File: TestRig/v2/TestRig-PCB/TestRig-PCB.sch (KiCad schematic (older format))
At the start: 1 part

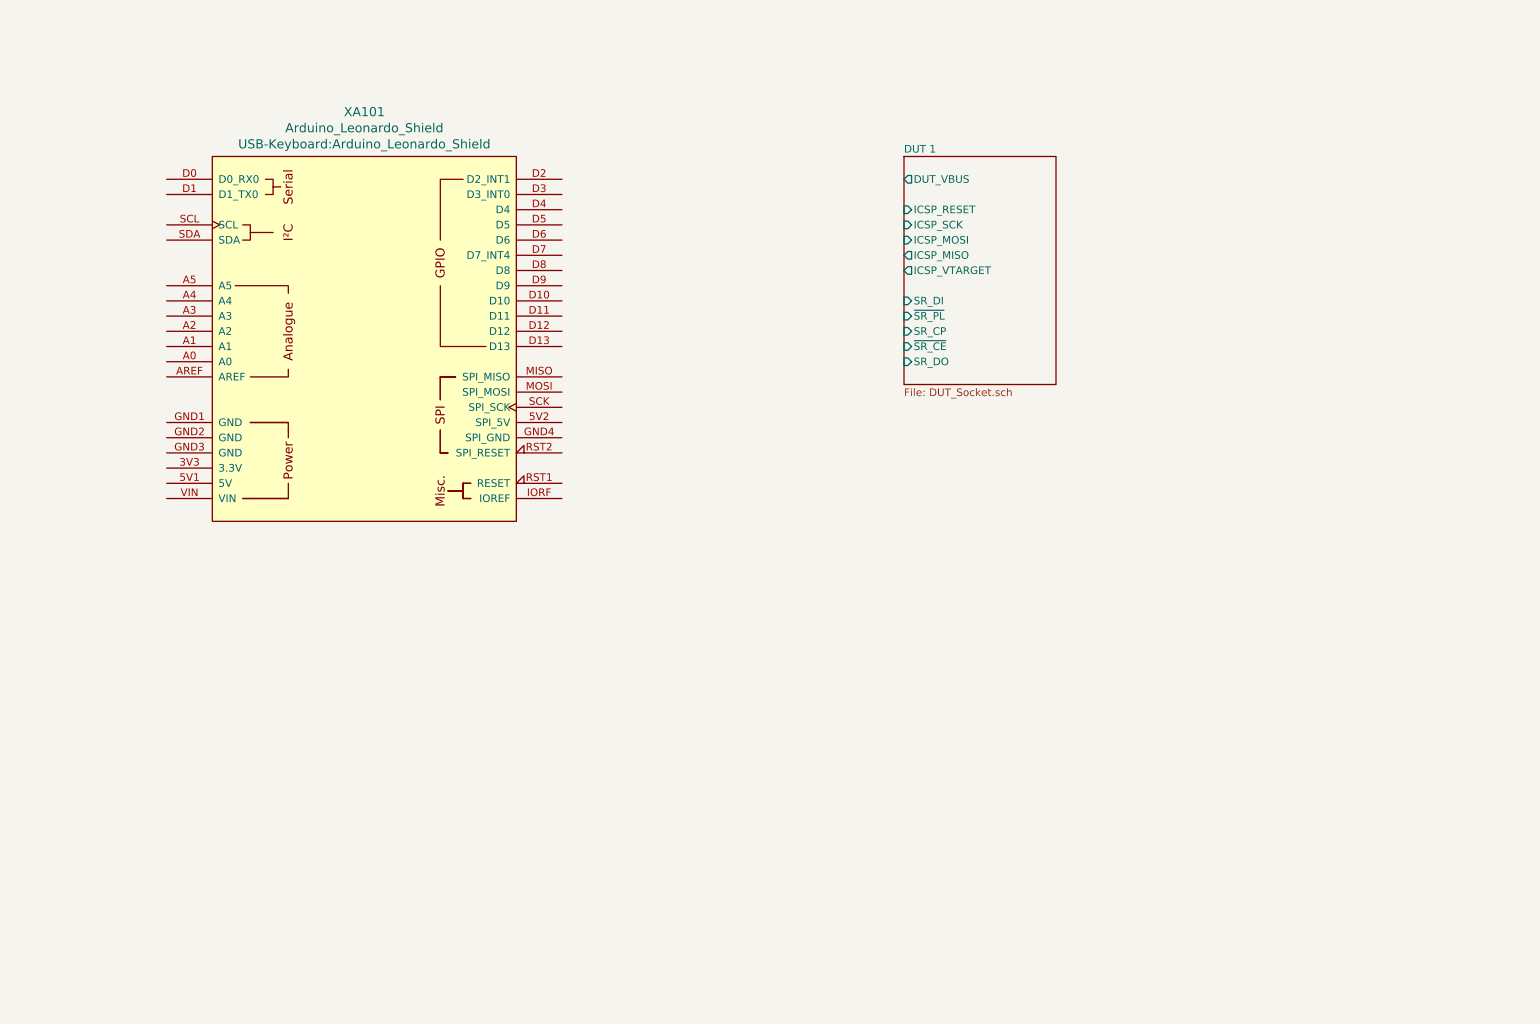
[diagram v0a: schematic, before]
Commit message: Adds working test rig
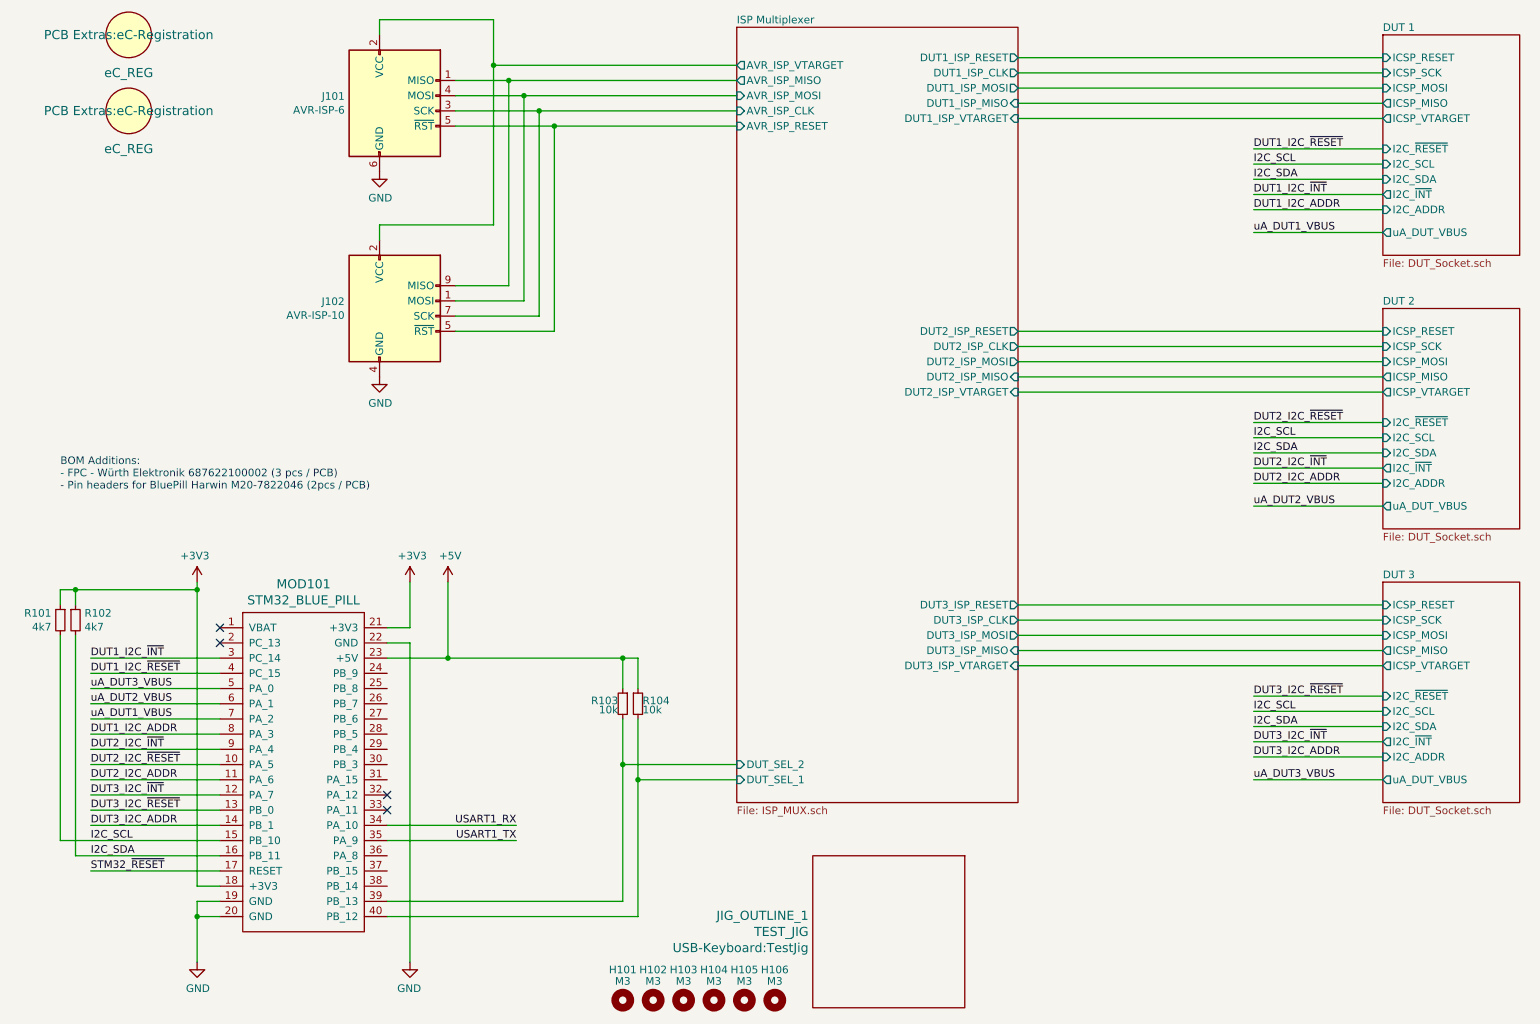
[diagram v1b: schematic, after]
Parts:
- removed XA101: Arduino_Leonardo_Shield, USB-Keyboard:Arduino_Leonardo_Shield, symbol arduino:Arduino_Leonardo_Shield
- added H101, H102, H103, H104, H105, H106: M3, MountingHole:MountingHole_3.2mm_M3, symbol Mechanical:MountingHole
- added J101: AVR-ISP-6, Connector_IDC:IDC-Header_2x03_P2.54mm_Vertical, symbol Connector:AVR-ISP-6
- added J102: AVR-ISP-10, Connector_IDC:IDC-Header_2x05_P2.54mm_Vertical, symbol Connector:AVR-ISP-10
- added JIG_OUTLINE_1: TEST_JIG, USB-Keyboard:TestJig, symbol rbv_pcb_extras:PCB_OUTLINE
- added MOD101: STM32_BLUE_PILL, BluePill:STM32F103C8T6-ARM-BOARD, symbol I2C-HID-Keyboard-rescue:STM32F103C8T6_BOARD
- added R101, R102: 4k7, Resistor_SMD:R_0603_1608Metric, symbol Device:R_Small
- added R103, R104: 10k, Resistor_SMD:R_0603_1608Metric, symbol Device:R_Small
- added REG101, REG102: eC_REG, PCB Extras:eC-Registration, symbol rbv_pcb_extras:DUMMY_KEY
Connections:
- new net +3V3: MOD101.18 (+3V3), MOD101.21 (+3V3), R101.1, R102.1
- new net +5V: MOD101.23 (+5V), R103.1, R104.1
- new net DUT1_I2C_ADDR: MOD101.8 (PA_3)
- new net DUT1_I2C_~INT: MOD101.3 (PC_14)
- new net DUT1_I2C_~RESET: MOD101.4 (PC_15)
- new net DUT2_I2C_ADDR: MOD101.11 (PA_6)
- new net DUT2_I2C_~INT: MOD101.9 (PA_4)
- new net DUT2_I2C_~RESET: MOD101.10 (PA_5)
- new net DUT3_I2C_ADDR: MOD101.14 (PB_1)
- new net DUT3_I2C_~INT: MOD101.12 (PA_7)
- new net DUT3_I2C_~RESET: MOD101.13 (PB_0)
- new net GND: J101.6 (GND), J102.10 (GND), J102.4 (GND), J102.6 (GND), J102.8 (GND), MOD101.19 (GND), MOD101.20 (GND), MOD101.22 (GND)
- new net I2C_SCL: MOD101.15 (PB_10), R101.2
- new net I2C_SDA: MOD101.16 (PB_11), R102.2
- new net ISP Multiplexer/AVR_ISP_CLK: J101.3 (SCK), J102.7 (SCK)
- new net ISP Multiplexer/AVR_ISP_MISO: J101.1 (MISO), J102.9 (MISO)
- new net ISP Multiplexer/AVR_ISP_MOSI: J101.4 (MOSI), J102.1 (MOSI)
- new net ISP Multiplexer/AVR_ISP_RESET: J101.5 (~RST), J102.5 (~RST)
- new net ISP Multiplexer/AVR_ISP_VTARGET: J101.2 (VCC), J102.2 (VCC)
- new net ISP Multiplexer/DUT_SEL_1: MOD101.40 (PB_12), R104.2
- new net ISP Multiplexer/DUT_SEL_2: MOD101.39 (PB_13), R103.2
- new net STM32_~RESET: MOD101.17 (RESET)
- new net USART1_RX: MOD101.34 (PA_10)
- new net USART1_TX: MOD101.35 (PA_9)
- new net uA_DUT1_VBUS: MOD101.7 (PA_2)
- new net uA_DUT2_VBUS: MOD101.6 (PA_1)
- new net uA_DUT3_VBUS: MOD101.5 (PA_0)
- no-connect marks 0 -> 4
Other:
- note added: "BOM Additions:\n- FPC - Würth Elektronik 687622100002 (3 pcs / PCB)\n- Pin headers for BluePill Harwin M20-7822046 (2pcs / PCB)"
